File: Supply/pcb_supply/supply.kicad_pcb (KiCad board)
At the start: 2 copper layers, 89.5 x 36.2 mm, 31 parts, among them J1 Screw_Terminal_01x02, J2 Screw_Terminal_01x02, Q1 FDS4685, U1 LTC3864

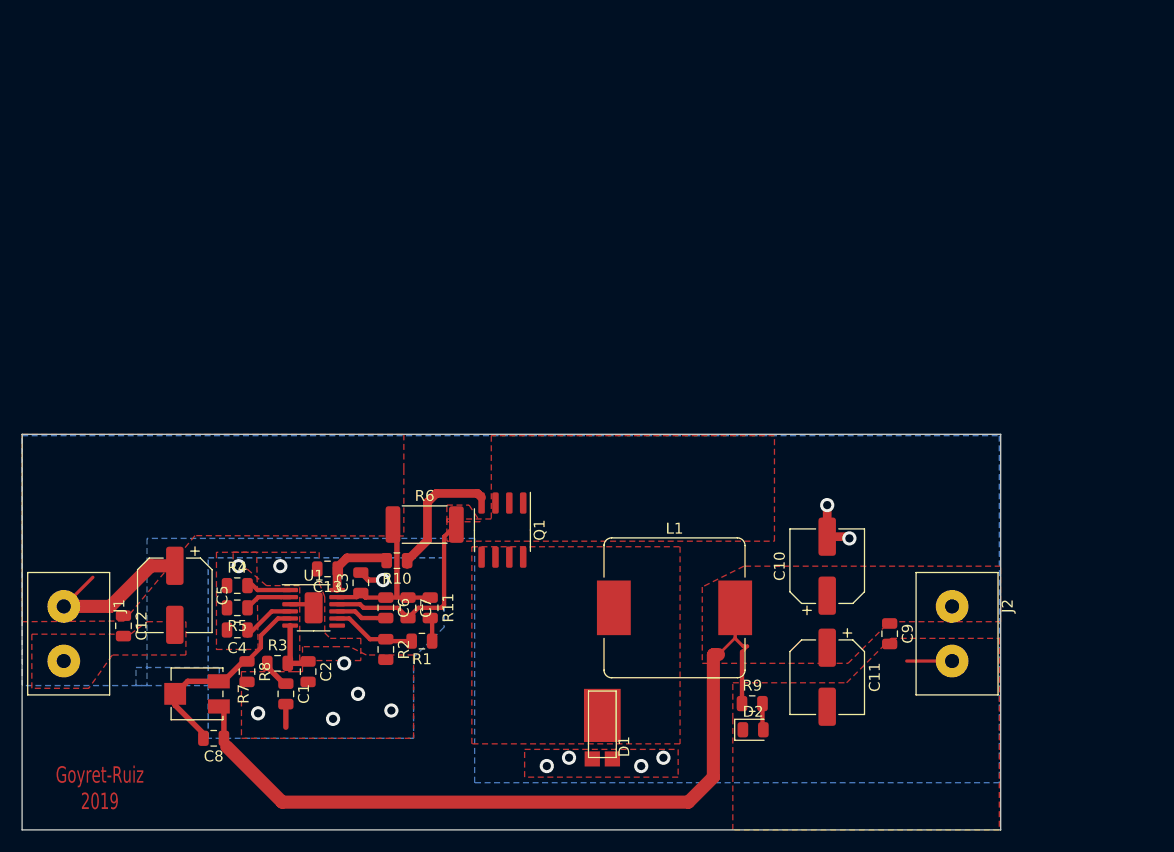
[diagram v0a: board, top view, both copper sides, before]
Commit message: Comienzo con la 3ra revisión de la fuente de switching
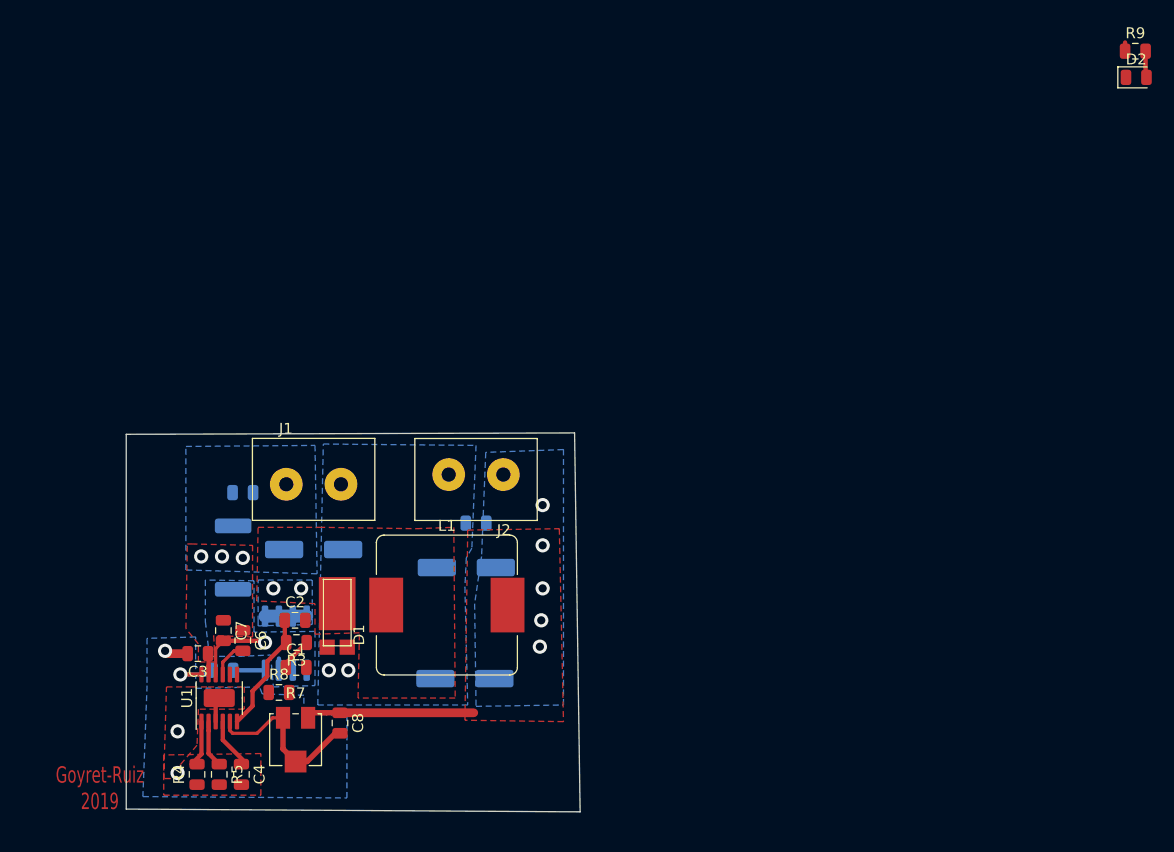
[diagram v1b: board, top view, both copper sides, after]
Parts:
- removed C13: 22p, Capacitor_SMD:C_0805_2012Metric
- removed R1: 390K, Resistor_SMD:R_0805_2012Metric
- removed R11: 0, Resistor_SMD:R_0805_2012Metric
- removed R2: 33K, Resistor_SMD:R_0805_2012Metric
- C10, C11, C12, C5, C9, Q1, R10, R6: moved to B.Cu
- moved R9 69.2 mm to (207.3, 36.7)
- moved D2 69.2 mm to (207.3, 39.1)
- moved J2 45.9 mm to (146.9, 75.4), turned to 180 degrees
- moved C9 39.2 mm to (146.9, 79.9), turned to 180 degrees
- moved C10 34.7 mm to (145.9, 94.1), turned to 180 degrees
- moved C11 34.5 mm to (146.1, 83.9), turned to 180 degrees
- moved J1 26.6 mm to (132.1, 76.3), turned to 0 degrees
- moved D1 26.3 mm to (134.2, 90.1)
- moved Q1 22.4 mm to (129.5, 90.9), turned to 90 degrees
- moved L1 20.8 mm to (144.3, 87.4)
- moved R10 18.8 mm to (123.8, 93.3)
- moved R6 17.8 mm to (124.7, 83.0), turned to 270 degrees
- moved R4 17.7 mm to (121.4, 102.9), turned to 90 degrees
- moved C7 17.0 mm to (123.8, 89.7)
- moved C12 16.4 mm to (125.6, 77.1), turned to 0 degrees
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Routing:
- net /VOUT: track 77.5 -> 16.1 mm, vias 0 -> 5
- net VDC: track 31.1 -> 2.71 mm, vias 0 -> 3
- net GND: track 15.6 -> 4.45 mm, vias 14 -> 5
- net Net-(C7-Pad2): track 19.1 -> 8.95 mm, vias 0 -> 1
- net Net-(Q1-Pad4): track 12.2 -> 2.92 mm
- net Net-(U1-Pad8): track 7.68 -> 0.00 mm
- net Net-(C2-Pad1): track 5.41 -> 11.2 mm
- net Net-(D1-Pad1): track 0.00 -> 3.81 mm, vias 0 -> 2
- net Net-(C8-Pad2): track 19.2 -> 16.4 mm
- net Net-(R1-Pad1): track 2.18 -> 0.00 mm
- net Net-(R10-Pad2): track 6.91 -> 5.04 mm, vias 0 -> 1
- net Net-(C6-Pad2): track 4.71 -> 3.40 mm
- added copper zone on B.Cu, net /VOUT
- added copper zone on B.Cu, net Net-(C7-Pad2)
- added copper zone on B.Cu, net Net-(D1-Pad1)
- added copper zone on B.Cu, net VDC
- removed copper zone on F.Cu, net Net-(C7-Pad2)
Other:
- board size 89.5 x 36.2 mm -> 41.5 x 34.7 mm
- net class Default: trace_width 0.25 -> 0.6096; via_dia 0.8 -> 1.3; via_drill 0.4 -> 0.75

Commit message: Comienzo con la 3ra revisión de la fuente de switching(2)
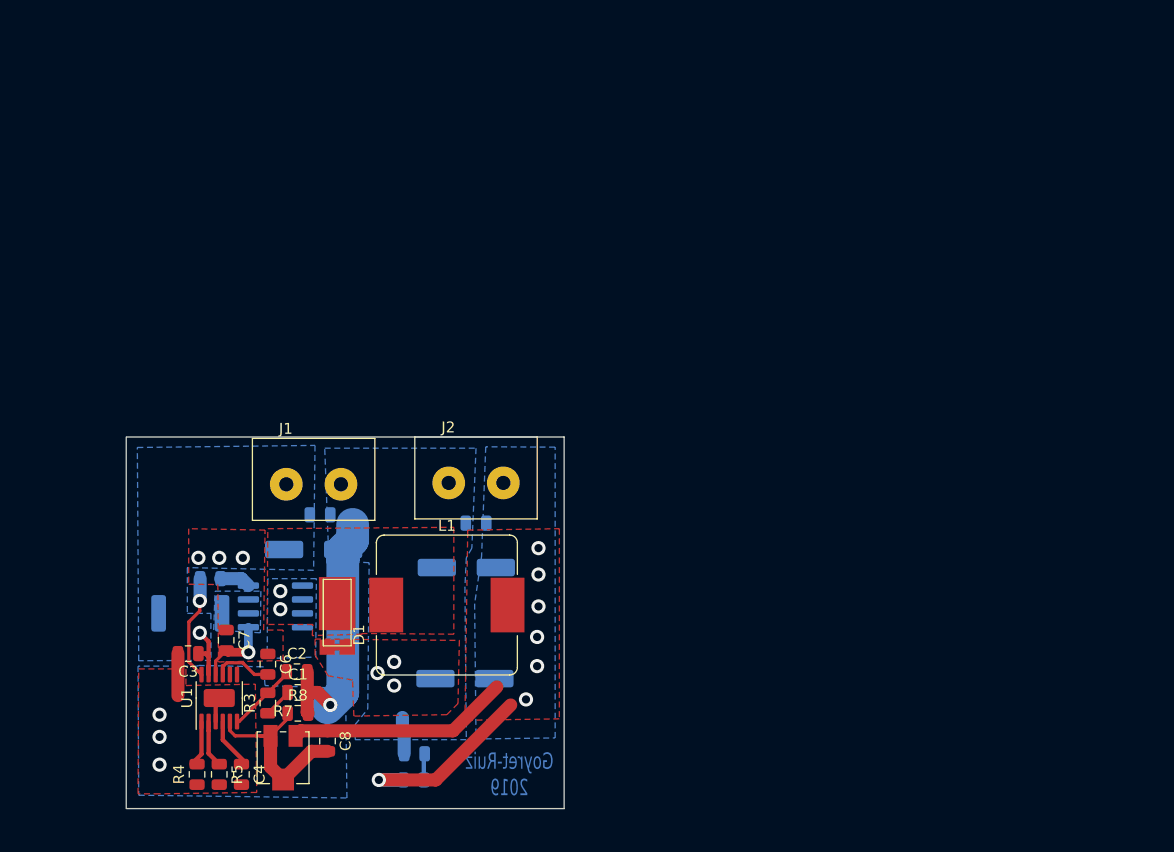
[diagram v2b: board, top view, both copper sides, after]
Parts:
- D2, R9: moved to B.Cu
- moved R9 93.8 mm to (141.2, 103.4)
- moved D2 90.5 mm to (141.3, 101.0)
- moved R10 8.46 mm to (122.6, 85.0)
- moved C12 7.35 mm to (132.7, 79.1)
- moved R6 6.43 mm to (120.8, 88.1), turned to 0 degrees
- moved R3 6.13 mm to (127.9, 96.3), turned to 90 degrees
- moved C2 4.70 mm to (130.6, 93.5)
- moved Q1 3.50 mm to (128.6, 87.5), turned to 0 degrees
- moved C6 3.14 mm to (127.9, 92.8)
- moved R8 2.57 mm to (130.6, 97.3)
- moved C1 2.29 mm to (130.6, 95.4)
- moved R7 2.01 mm to (129.3, 101.3)
- moved C8 2.01 mm to (133.3, 99.8)
- moved C7 0.92 mm to (124.1, 90.6)
- moved C3 0.89 mm to (120.6, 91.8)
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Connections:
- J2 pad 1: /VOUT -> GND
- J2 pad 2: GND -> /VOUT
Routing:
- net GND: track 4.45 -> 35.4 mm, vias 5 -> 7
- net /VOUT: track 16.1 -> 37.4 mm, vias 5 -> 7
- net Net-(R10-Pad2): track 5.04 -> 10.1 mm
- net Net-(C2-Pad1): track 11.2 -> 6.56 mm
- net Net-(D1-Pad1): track 3.81 -> 0.00 mm
- net VDC: track 2.71 -> 5.99 mm, vias 3 -> 4
- net Net-(C8-Pad2): track 16.4 -> 18.9 mm
- net Net-(C6-Pad2): track 3.40 -> 5.49 mm
- net Net-(C7-Pad2): track 8.95 -> 6.98 mm
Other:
- board size 41.5 x 34.7 mm -> 40.1 x 34 mm
